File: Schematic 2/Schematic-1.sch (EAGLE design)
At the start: 2 parts

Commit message: Schematic-2 Final
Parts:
- added R1, R2, R3: 4.7K, rcl:R-US_0204/5
- added R10, R11, R12, R13, R14, R15, R16, R17, R18, R19: (no value), adafruit:R-US_M1206
- added R4, R5: 1K, rcl:R-US_0204/5
- added U$4: ADC128D818, ADC128D818:ADC128D818
- added U2: LMV358, SparkFun-IC-Amplifiers:LMV358SOIC
- added U3: LMV324, SparkFun-IC-Amplifiers:LMV324
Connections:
- removed net N$3: U$1.3, U$1.3'
- removed net N$67: U$2.PA6
- removed net N$68: U$2.PA7
- removed net N$7: U$2.3.3V
- new net 3.3V: U$2.3.3V, U$4.VREF
- new net 5V1: U2G3.P$V+, U3G5.P$V+
- new net GND1: R10.2, R13.2, R15.2, R17.2, R19.2, U2G3.P$V-, U3G5.P$V-
- new net HGHJ: R11.2, U2G1.-IN, U2G1.OUT
- new net N$16: R1.1, R3.2, U$4.V+
- new net N$17: R3.1, U$4.INT
- new net N$18: R5.2, U$4.A0
- new net N$19: R4.2, U$4.A1
- new net N$2: U2G2.-IN, U2G2.OUT
- new net N$31: R4.1, R5.1
- new net N$8: R18.2, U3G4.-IN, U3G4.OUT
- new net N$9: R18.1, R19.1
- new net PB4: R10.1, R11.1
- new net PD3: R16.1, R16.2, R17.1, U3G3.-IN, U3G3.OUT
- new net PE0: R12.1, R12.2, R13.1, U3G1.-IN, U3G1.OUT
- new net PE2: R14.1, R14.2, R15.1, U3G2.-IN, U3G2.OUT
- new net SCL: R2.2, U$2.PA6, U$4.SCL
- new net SDA: R1.2, U$2.PA7, U$4.SDA
- new net SHARP1: U3G1.+IN
- new net SHARP2: U3G2.+IN
- new net SHARP3: U3G3.+IN
- new net SHARP4: U3G4.+IN
- new net SHARP5: U2G1.+IN
- net 15: now also U$4.IN1
- net 2: now also U$4.IN0
- net 36: now also U$4.IN2
- net 37: now also U$4.IN3
- net 38: now also U$4.IN4
- net 39: now also U$4.IN5
- net 44: now also U$4.IN6
- net 69: now also U$4.IN7
- net GND: now also U$1.3, U$1.3', U$4.GND

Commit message: Final changes to Schematic 2
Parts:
- added Q1, Q2: BSS138, SparkFun:MOSFET-NCHANNELSMD
- added R20, R21, R22, R23: 10K, SparkFun:RESISTOR1206
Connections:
- removed net GND1: R10.2, R13.2, R15.2, R17.2, R19.2, U2G3.P$V-, U3G5.P$V-
- removed net N$50: U$1.63, U$1.63'
- new net 63: Q2.D, R23.2, U$1.63, U$1.63'
- new net N$3: U2G2.+IN
- new net PB2: Q1.S, R20.2, U$2.PB2
- new net PF0: Q2.S, R22.2, U$2.PF0
- new net POWER5: R21.1, R23.1
- new net VDD: Q1.G, Q2.G, R20.1, R22.1
- net 61: no longer U$2.PB2
- net 62: now also Q1.D, R21.2; no longer U$2.PF0
- net GND: now also R10.2, R13.2, R15.2, R17.2, R19.2, U2G3.P$V-, U3G5.P$V-
- net N$16: now also R2.1
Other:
- moved on the sheet: R1, R10, R11, R12, R13, R14, R15, R16, R17, R18, R19, R2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

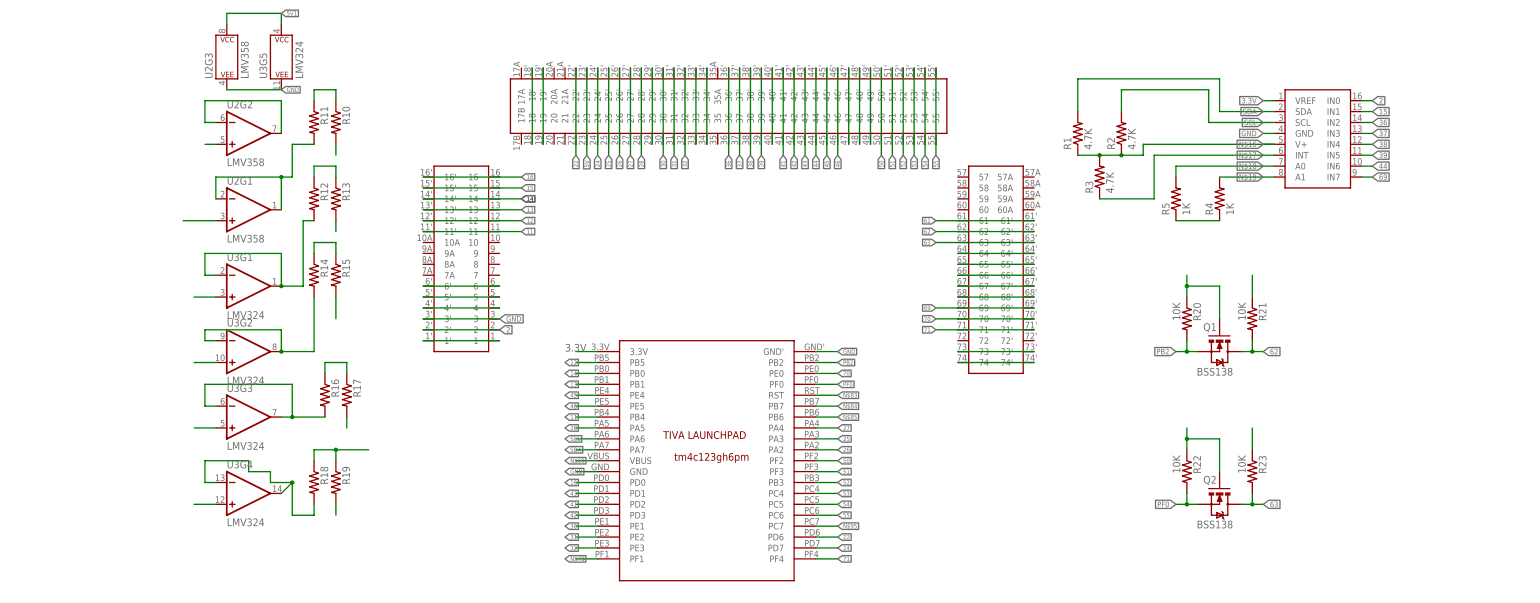
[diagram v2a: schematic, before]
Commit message: Layout of daughter board
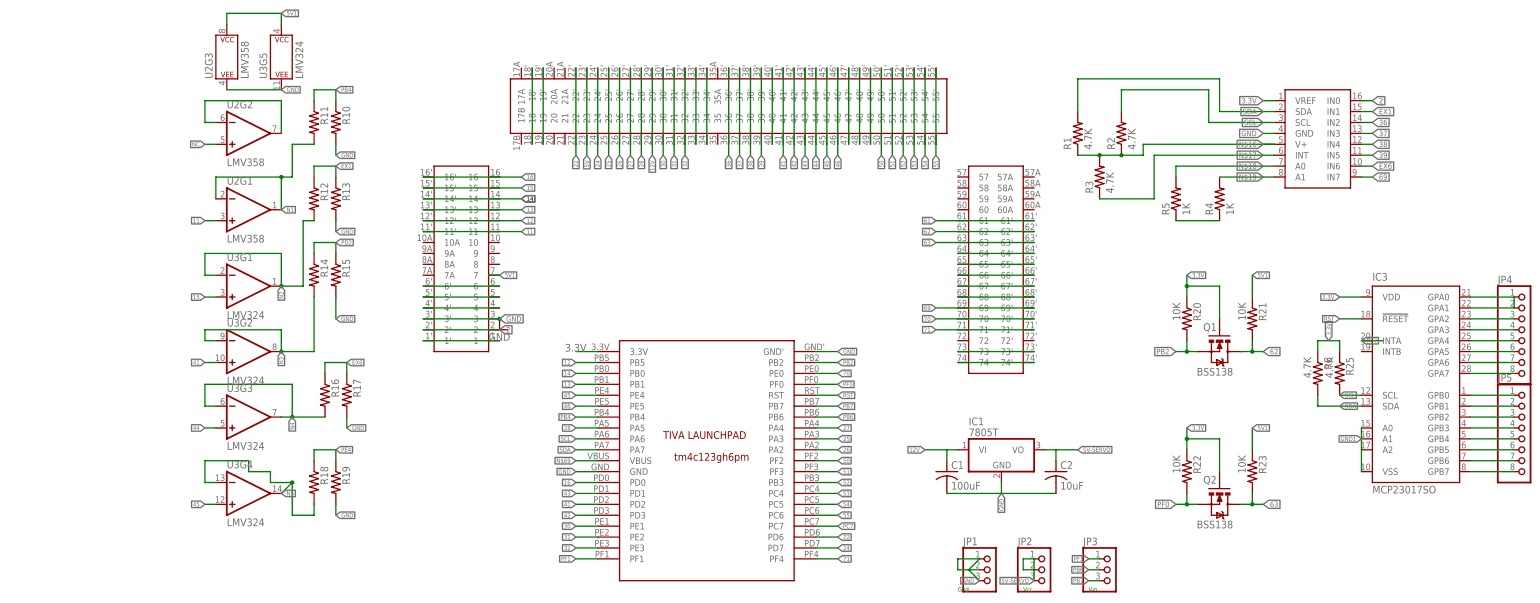
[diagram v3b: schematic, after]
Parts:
- added C1: 100uF, adafruit:C-US025-030X050
- added C2: 10uF, adafruit:C-US025-030X050
- added IC1: 7805T, adafruit:7805T
- added IC3: MCP23017SO, adafruit:MCP23017SO
- added JP1, JP2, JP3: (no value), adafruit:PINHD-1X3
- added JP4, JP5: (no value), adafruit:PINHD-1X8BIG
- added R25, R6: 4.7K, adafruit:R-US_M1206
- R1, R2, R3, R4, R5: device rcl:R-US_0204/5 -> rcl:R-US_M1206
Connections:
- net HGHJ renamed N1
- net N$3 renamed NC
- net N$8 renamed N5
- net N$9 renamed PE4
- removed net N$78: U$2.PF1
- removed net N$83: U$2.RST
- removed net N$84: U$2.PB7
- removed net N$85: U$2.PB6
- removed net N$95: U$2.PC7
- removed net PD3: R16.1, R16.2, R17.1, U3G3.-IN, U3G3.OUT
- removed net PE0: R12.1, R12.2, R13.1, U3G1.-IN, U3G1.OUT
- removed net PE2: R14.1, R14.2, R15.1, U3G2.-IN, U3G2.OUT
- removed net POWER5: R21.1, R23.1
- removed net SHARP1: U3G1.+IN
- removed net SHARP2: U3G2.+IN
- removed net SHARP3: U3G3.+IN
- removed net SHARP4: U3G4.+IN
- removed net SHARP5: U2G1.+IN
- removed net VDD: Q1.G, Q2.G, R20.1, R22.1
- new net 12V: C1.1, IC1.VI, U$1.29, U$1.29'
- new net 5V-SERVO: C2.1, IC1.VO, JP2.1, JP2.2, JP2.3
- new net EX1: R12.1, R13.1, U$4.IN1
- new net EX6: R16.1, R17.1, U$4.IN6
- new net GND1: IC3.A0, IC3.A2, IC3.VSS
- new net N$10: IC3.GPA4, JP4.5
- new net N$11: IC3.GPA5, JP4.6
- new net N$12: IC3.GPA6, JP4.7
- new net N$15: IC3.GPA7, JP4.8
- new net N$20: IC3.GPB0, JP5.1
- new net N$21: IC3.GPB1, JP5.2
- new net N$23: IC3.GPB3, JP5.4
- new net N$24: IC3.GPB4, JP5.5
- new net N$25: IC3.GPB5, JP5.6
- new net N$28: IC3.GPB6, JP5.7
- new net N$29: IC3.GPB7, JP5.8
- new net N$3: IC3.GPA0, IC3.GPA1, JP4.1
- new net N$7: IC3.GPA2, JP4.3
- new net N$8: IC3.GPA3, JP4.4
- new net N2: R12.2, U3G1.-IN, U3G1.OUT
- new net N3: R14.2, U3G2.-IN, U3G2.OUT
- new net N4: R16.2, U3G3.-IN, U3G3.OUT
- new net PB6: JP3.2, U$2.PB6
- new net PB7: JP3.3, U$2.PB7
- new net PC7: IC3.INTA, U$2.PC7
- new net PD2: R14.1, R15.1
- new net PF1: JP3.1, U$2.PF1
- new net RST: IC3.!RESET, U$2.RST
- net 11: now also U2G1.+IN; no longer U$2.PB4
- net 15: now also U3G1.+IN; no longer U$4.IN1
- net 3.3V: now also IC3.VDD, Q1.G, Q2.G, R20.1, R22.1, R25.1, R6.1
- net 41: now also U3G2.+IN
- net 44: now also U3G3.+IN; no longer U$4.IN6
- net 45: now also U3G4.+IN
- net 5V1: now also R21.1, R23.1, U$1.7
- net GND: now also C1.2, C2.2, IC1.GND, JP1.1, JP1.2, JP1.3
- net N$22: now also IC3.GPB2, JP5.3; no longer U$1.29, U$1.29'
- net PB4: now also U$2.PB4
- net SCL: now also IC3.SCL, R25.2
- net SDA: now also IC3.SDA, R6.2
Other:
- note added: "Gnd"
- note added: "Vcc"
- note added: "Vin"
